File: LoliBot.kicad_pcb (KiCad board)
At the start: 2 copper layers, 146 x 100 mm, 41 parts, among them J1 LOLINBATT, J10 LEFT-MOTOR, J11 REFLECT_, J12 MECH, J13 MECH, J14 MECH, J15 MECH, J16 MECH, J17 MECH, J18 MECH, J19 MECH, J2 APA106, J20 CONN_01X08, J21 CONN_01X06, J22 BRIDGE, J23 BRIDGE, J24 FUSE_BRIDGE, J25 MECH, J26 MECH, J27 MECH, J28 MECH, J29 MECH, J3 SERVO1, J30 MECH, J4 RIGHT, J5 LEFT, J6 MPU-9250, J7 APA106, J8 APA106, J9 RIGHT-MOTOR, SW1 SPST, U1 LOLIN32-LITE, U3 L9110, U4 L9110

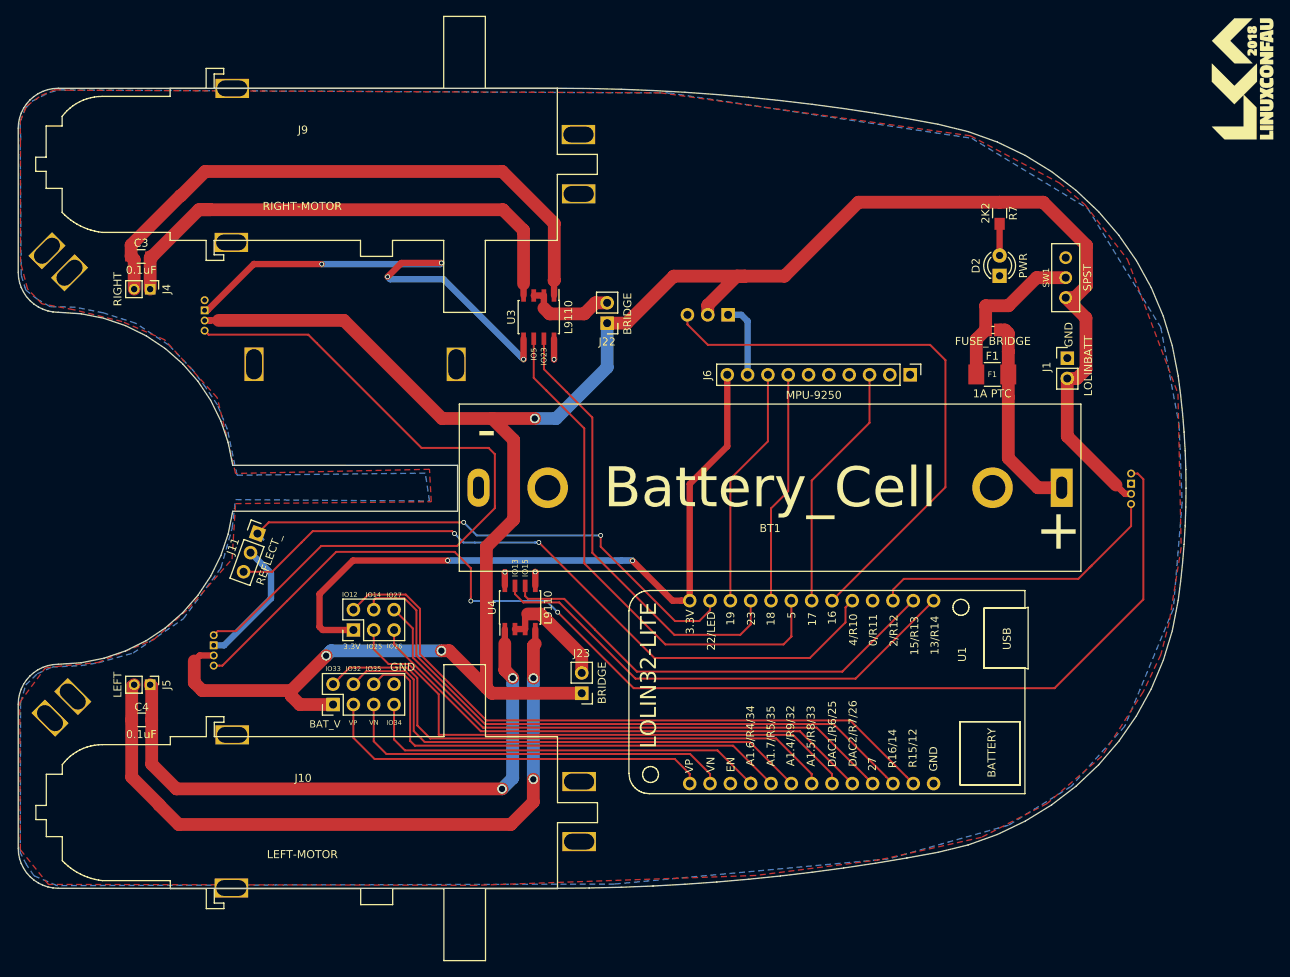
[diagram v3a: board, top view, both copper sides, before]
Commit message: Added logos and text
And vias.
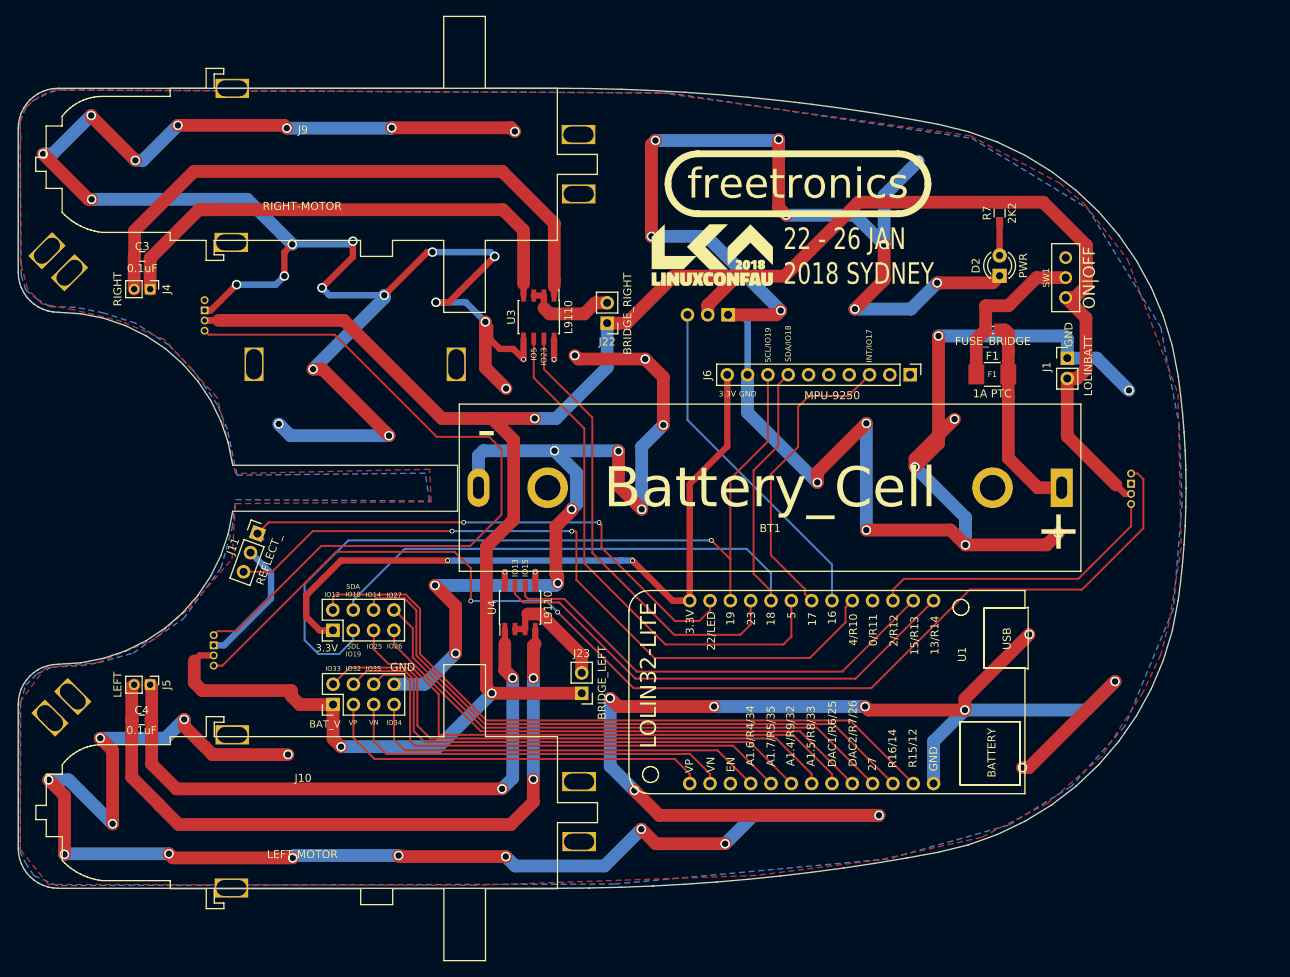
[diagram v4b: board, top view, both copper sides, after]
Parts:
- removed G***: LOGO, libs:LCA2018_LOGO
- added J31: LCA_LOGO, libs:LCA2018_LOGO, F.Cu at (137.7, 60.1)
- added J32: FREETRONICS_LOGO, libs:LOGO_FREETRONICS_33mm, F.Cu at (148.5, 51.2)
- C3, C4: footprint Capacitors_SMD:C_0805_HandSoldering -> Capacitors_SMD:C_0603_HandSoldering
- J21: value CONN_01X06 -> CONN_01X08; footprint Pin_Headers:Pin_Header_Straight_2x03_Pitch2.54mm -> Pin_Headers:Pin_Header_Straight_2x04_Pitch2.54mm
- J22: value BRIDGE -> BRIDGE_RIGHT
- J23: value BRIDGE -> BRIDGE_LEFT
- R7: footprint Resistors_SMD:R_0805_HandSoldering -> Resistors_SMD:R_0603_HandSoldering
- SW1: value SPST -> ON|OFF
- moved J21 2.57 mm to (90.3, 107.0)
- moved C3 0.14 mm to (66.5, 60.3)
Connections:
- J21 pad 3: /IO25 -> /IO19
- J21 pad 4: /IO14 -> /IO18
- J21 pad 5: /IO26 -> /IO25
- J21 pad 6: /IO27 -> /IO14
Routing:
- net GND: track 95.2 -> 945.1 mm, vias 7 -> 75
- net /IO19: track 30.3 -> 102.5 mm, vias 0 -> 1
- net /IO18: track 28.9 -> 91.7 mm
- net /IO16: track 71.2 -> 43.2 mm
- net /INT: track 31.2 -> 38.3 mm
- net Net-(J2-Pad4): track 153.0 -> 147.8 mm
- net /IO12: track 83.9 -> 87.4 mm
- net /IO4: track 88.8 -> 92.3 mm
- net Net-(J7-Pad4): track 91.1 -> 93.6 mm
- net /BATT_V: track 291.3 -> 290.2 mm
- net /IO22: track 65.9 -> 66.7 mm
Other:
- board text added: "22 - 26 JAN 2018 SYDNEY"
- board text added: "Designed by John Spencer Made by freetronics.com.au © 2017 John Spencer License TAPR OHL v1.0"
- board text added: "INT/IO17"
- board text added: "Lolibot V1.2"
- board text added: "SCL/IO19"
- board text added: "SDA IO18"
- board text added: "SDA/IO18"
- board text added: "SDL IO19"
- board text added: "github.com/CCHS-Melbourne/LoliBot"

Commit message: Added more text
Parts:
- BT1: value Battery_Cell -> BATTERY
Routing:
- net /IO16: vias 0 -> 1
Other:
- board text added: "IO22"
- board text added: "IO4"
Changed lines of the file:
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@@
     (area 50.929999 39.209999 197.009248 139.310001)
     (thickness 1.6)
-    (drawings 216)
-    (tracks 619)
+    (drawings 220)
+    (tracks 623)
     (zones 0)
     (modules 42)
@@
   )
   (setup
-    (last_trace_width 1.6)
+    (last_trace_width 0.25)
     (user_trace_width 0.6)
     (user_trace_width 0.8)
@@
       (effects (font (size 1 1) (thickness 0.15)))
     )
-    (fp_text value Battery_Cell (at 0 0) (layer F.SilkS)
+    (fp_text value BATTERY (at 0 0) (layer F.SilkS)
       (effects (font (size 5 5) (thickness 1)))
     )
@@
   (module libs:DC-Motor locked (layer F.Cu)
     (at 86.49 48.87 180)
-    (fp_text reference J9 (at -0.08 4.41 180) (layer F.SilkS)
-      (effects (font (size 1 1) (thickness 0.15)))
-    )
-    (fp_text value RIGHT-MOTOR (at 0.01 -5.13 180) (layer F.SilkS)
-      (effects (font (size 1 1) (thickness 0.15)))
+    (fp_text reference J9 (at 30.3306 0.20868 180) (layer F.SilkS)
+      (effects (font (size 1 1) (thickness 0.15)))
+    )
+    (fp_text value RIGHT-MOTOR (at 0.16556 0.40172 180) (layer F.SilkS)
+      (effects (font (size 3 3) (thickness 0.5)))
     )
     (fp_line (start 33.3211 -0.775733) (end 33.3211 0.9936) (layer F.SilkS) (width 0.1))
@@
   (module libs:DC-Motor locked (layer F.Cu)
     (at 86.51 129.9 180)
-    (fp_text reference J10 (at -0.08 4.41 180) (layer F.SilkS)
-      (effects (font (size 1 1) (thickness 0.15)))
-    )
-    (fp_text value LEFT-MOTOR (at 0.01 -5.13 180) (layer F.SilkS)
-      (effects (font (size 1 1) (thickness 0.15)))
+    (fp_text reference J10 (at 30.43696 0.1568 180) (layer F.SilkS)
+      (effects (font (size 1 1) (thickness 0.15)))
+    )
+    (fp_text value LEFT-MOTOR (at -0.03288 0.02472 180) (layer F.SilkS)
+      (effects (font (size 3 3) (thickness 0.5)))
     )
     (fp_line (start 33.3211 -0.775733) (end 33.3211 0.9936) (layer F.SilkS) (width 0.1))
@@
     )
   )
+  (gr_text IO4 (at 80.95996 100.5078 340) (layer B.SilkS)
+    (effects (font (size 1 1) (thickness 0.2)) (justify right mirror))
+  )
+  (gr_text IO4 (at 78.36916 101.68128 340) (layer F.SilkS)
+    (effects (font (size 0.7 0.7) (thickness 0.175)))
+  )
+  (gr_text IO22 (at 81.77784 93.0656 340) (layer F.SilkS)
+    (effects (font (size 0.7 0.7) (thickness 0.175)))
+  )
+  (gr_text IO22 (at 85.81644 96.8248 340) (layer B.SilkS)
+    (effects (font (size 1 1) (thickness 0.2)) (justify left mirror))
+  )
   (gr_text "SDL\nIO19" (at 92.87764 109.50448) (layer B.SilkS)
     (effects (font (size 0.6 0.6) (thickness 0.15)) (justify mirror))
@@
     (effects (font (size 0.7 0.7) (thickness 0.175)) (justify right))
   )
-  (gr_text 3.3V (at 139.61872 77.45984 360) (layer B.SilkS)
+  (gr_text 3.3V (at 139.61872 77.45984) (layer B.SilkS)
     (effects (font (size 0.7 0.7) (thickness 0.175)) (justify mirror))
   )
-  (gr_text GND (at 142.17904 77.46492 360) (layer B.SilkS)
+  (gr_text GND (at 142.17904 77.46492) (layer B.SilkS)
     (effects (font (size 0.7 0.7) (thickness 0.175)) (justify mirror))
   )
@@
   (gr_line (start 52.013233 41.216193) (end 52.444466 40.724466) (layer Edge.Cuts) (width 0.1))
   (gr_line (start 126.342321 39.38536) (end 130.33114 39.542032) (layer Edge.Cuts) (width 0.1))
+  (via (at 113.0554 44.65828) (size 1.2) (drill 0.8) (layers F.Cu B.Cu) (net 1))
+  (segment (start 97.67316 44.196) (end 112.59312 44.196) (width 1.6) (layer F.Cu) (net 1))
+  (segment (start 112.59312 44.196) (end 113.0554 44.65828) (width 1.6) (layer F.Cu) (net 1))
   (segment (start 169.3164 116.98224) (end 169.3164 115.56492) (width 1.6) (layer F.Cu) (net 1))
   (segment (start 169.3164 115.56492) (end 177.34788 107.53344) (width 1.6) (layer F.Cu) (net 1))
@@
   (segment (start 165.4 120.89864) (end 169.3164 116.98224) (width 1.6) (layer B.Cu) (net 1))
   (via (at 169.3164 116.98224) (size 1.2) (drill 0.8) (layers F.Cu B.Cu) (net 1))
-  (segment (start 97.67316 44.196) (end 112.59312 44.196) (width 1.6) (layer F.Cu) (net 1))
-  (segment (start 112.59312 44.196) (end 113.0554 44.65828) (width 1.6) (layer F.Cu) (net 1))
-  (via (at 113.0554 44.65828) (size 1.2) (drill 0.8) (layers F.Cu B.Cu) (net 1))
   (segment (start 84.55152 44.2468) (end 97.62236 44.2468) (width 1.6) (layer B.Cu) (net 1))
   (segment (start 97.62236 44.2468) (end 97.67316 44.196) (width 1.6) (layer B.Cu) (net 1))
@@
   (segment (start 121.74 98.6432) (end 121.74 81.78072) (width 0.25) (layer F.Cu) (net 18))
   (segment (start 121.74 81.78072) (end 116.98732 77.02804) (width 0.25) (layer F.Cu) (net 18))
-  (segment (start 134.63524 67.57924) (end 134.63524 80.7212) (width 0.25) (layer B.Cu) (net 19))
-  (segment (start 134.63524 80.7212) (end 152.7 98.78596) (width 0.25) (layer B.Cu) (net 19))
+  (segment (start 137.06348 83.14944) (end 152.7 98.78596) (width 0.25) (layer B.Cu) (net 19))
+  (segment (start 134.6454 68.791481) (end 134.6454 80.73136) (width 0.25) (layer F.Cu) (net 19))
+  (segment (start 134.6454 80.73136) (end 137.06348 83.14944) (width 0.25) (layer F.Cu) (net 19))
+  (via (at 137.06348 83.14944) (size 0.6) (drill 0.4) (layers F.Cu B.Cu) (net 19))
+  (segment (start 134.63524 67.57924) (end 134.63524 68.781321) (width 0.25) (layer F.Cu) (net 19))
+  (segment (start 134.63524 68.781321) (end 134.6454 68.791481) (width 0.25) (layer F.Cu) (net 19))
   (segment (start 152.7 98.78596) (end 152.7 103.31) (width 0.25) (layer B.Cu) (net 19))
   (segment (start 114.086361 94.619801) (end 114.09172 94.62516) (width 0.25) (layer B.Cu) (net 20))

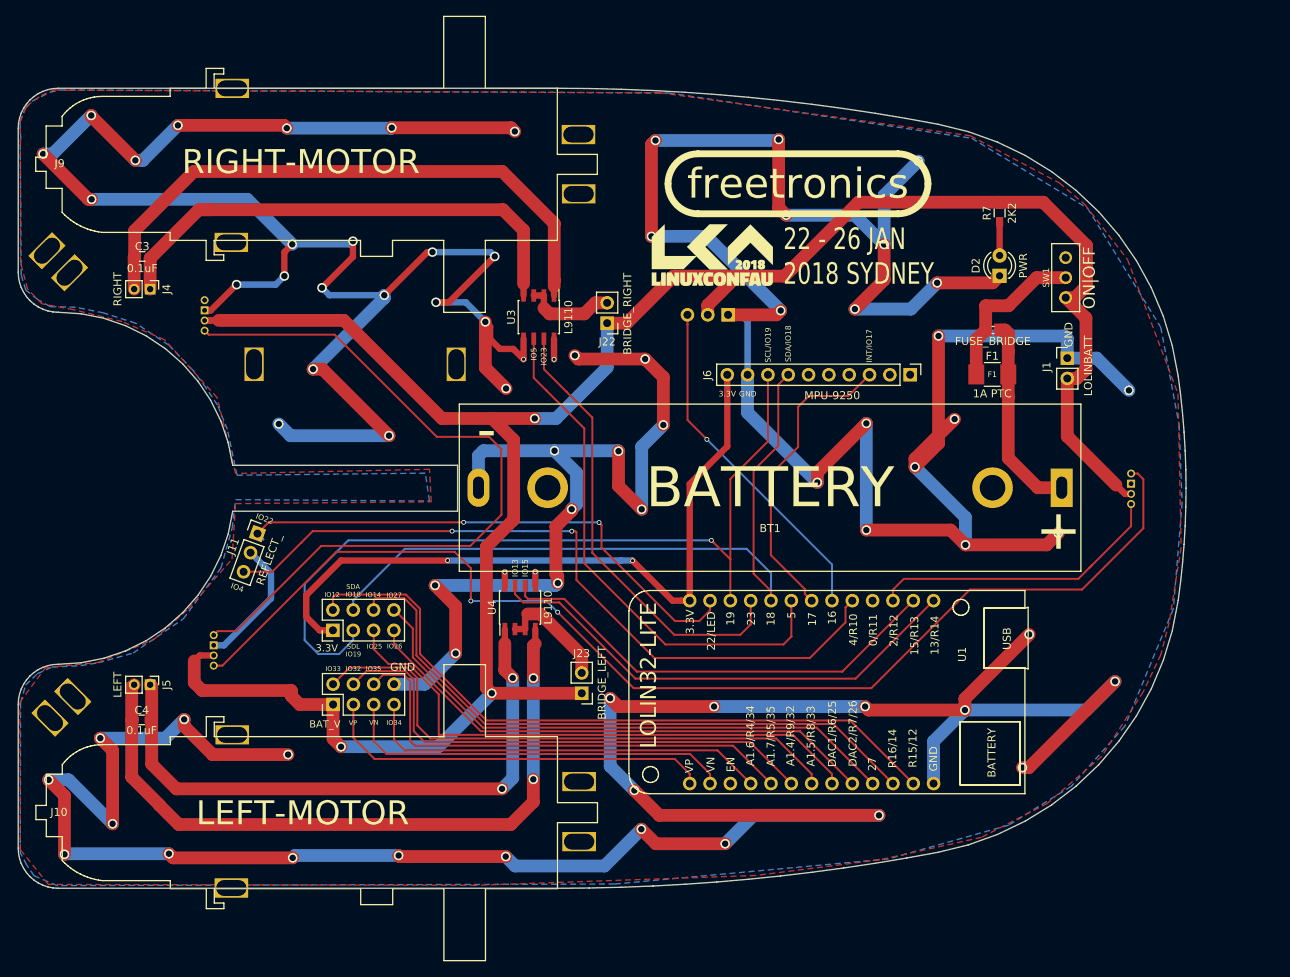
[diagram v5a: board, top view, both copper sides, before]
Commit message: i2c pullup resistors
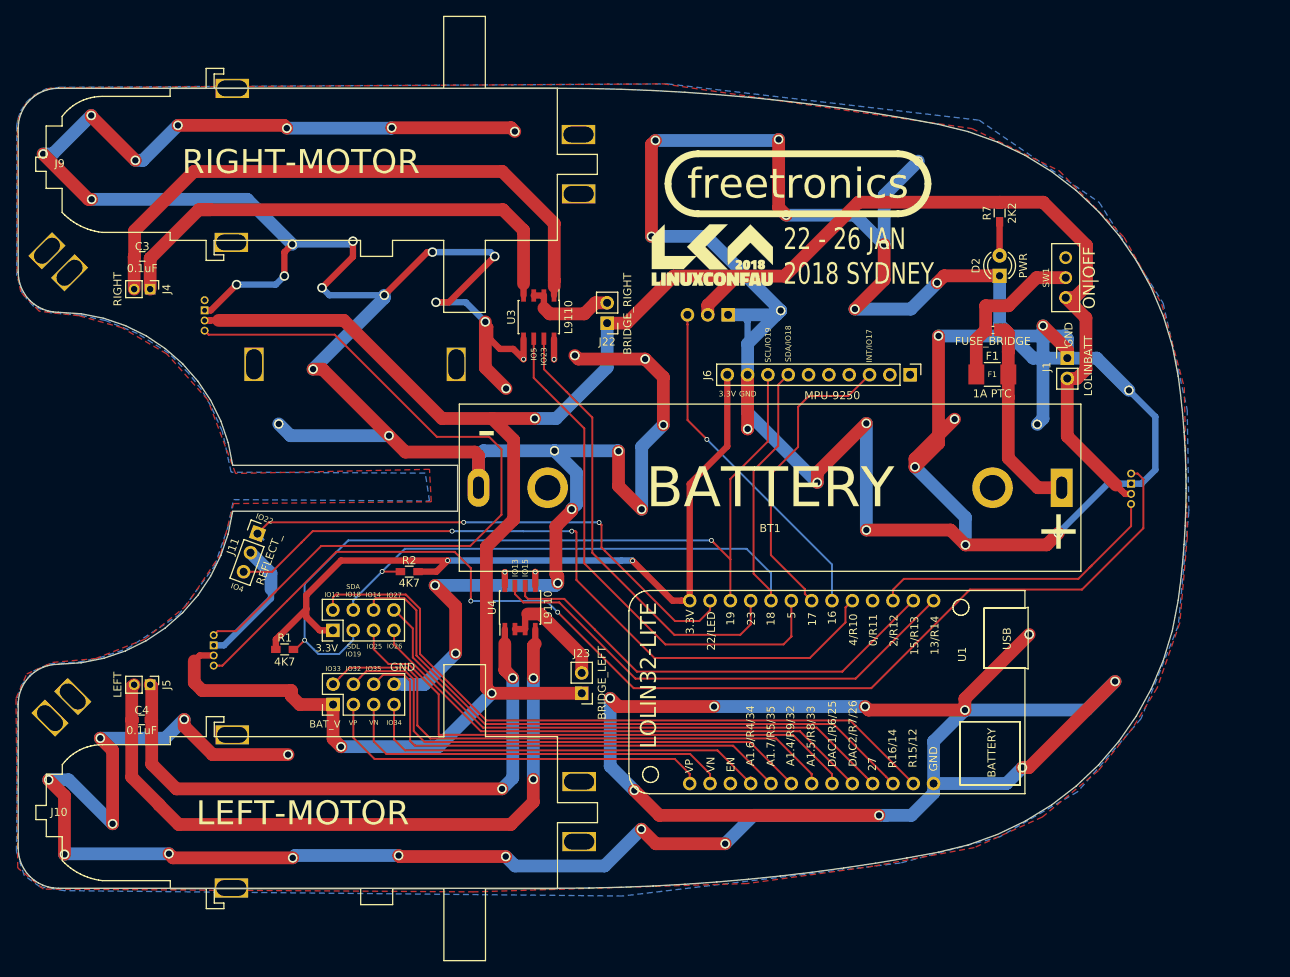
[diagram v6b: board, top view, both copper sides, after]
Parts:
- added R1: 4K7, Resistors_SMD:R_0603_HandSoldering, F.Cu at (84.3, 109.4)
- added R2: 4K7, Resistors_SMD:R_0603_HandSoldering, F.Cu at (99.9, 99.7)
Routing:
- net GND: track 945.1 -> 1059.9 mm, vias 75 -> 78
- net +3V3: track 88.7 -> 99.6 mm
- net /IO18: track 91.7 -> 94.0 mm, vias 0 -> 1
- net /IO19: track 102.5 -> 104.4 mm, vias 1 -> 2
